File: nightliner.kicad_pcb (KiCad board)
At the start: 2 copper layers, 79 parts, among them J1 TYPE-C-31-M-12, J2 Battery, SW1 SW_SPST, SW10 SW_SPST, SW11 SW_SPST, SW12 SW_SPST, SW13 SW_SPST, SW14 SW_SPST, SW15 SW_SPST, SW16 SW_SPST, SW17 SW_SPST, SW18 SW_SPST, SW19 SW_SPST, SW2 SW_SPST, SW20 SW_SPST, SW21 ON_OFF, SW22 RESET, SW23 BAT_CHECK, SW3 SW_SPST, SW4 SW_SPST, SW5 SW_SPST, SW6 SW_SPST, SW7 SW_SPST, SW8 SW_SPST, SW9 SW_SPST, U1 holyiot-18010, U2 TVS2200DRV, U3 USBLC6-2SC6, U4 BQ24075RGT, U5 XC6220B331MR

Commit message: feat: PCB placement (with wrong choc pos)
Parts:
- removed SW23: BAT_CHECK, miro_keyboard:SW_Push_1P1T_NO_CK_KSC4xxJ
- FB1: value Ferritebead -> Ferrite
- J2: footprint Connector_JST:JST_EH_B3B-EH-A_1x03_P2.50mm_Vertical -> Connector_JST:JST_EH_S3B-EH_1x03_P2.50mm_Horizontal
- SW21: footprint Button_Switch_SMD:SW_SPDT_PCM12 -> miro_keyboard:SW_XKB_SS-12D11_SPDT_Angled
- moved SW9 94.9 mm to (129.2, 69.1), turned to 0 degrees
- moved SW4 88.9 mm to (129.2, 50.9), turned to 0 degrees
- moved D20 87.5 mm to (155.4, 26.7), turned to 90 degrees
- moved SW11 86.9 mm to (33.9, 81.0), turned to 10 degrees
- moved D19 82.1 mm to (151.9, 26.7), turned to 90 degrees
- moved D15 81.6 mm to (155.4, 22.9), turned to 90 degrees
- moved D18 79.4 mm to (148.3, 26.7), turned to 90 degrees
- moved D16 78.3 mm to (141.2, 26.7), turned to 90 degrees
- moved D14 76.2 mm to (151.9, 22.9), turned to 90 degrees
- moved D10 75.8 mm to (155.4, 19.1), turned to 90 degrees
- moved SW16 75.6 mm to (37.0, 98.9), turned to 10 degrees
- moved D17 73.9 mm to (144.8, 26.7), turned to 90 degrees
- moved D13 73.0 mm to (148.3, 22.9), turned to 90 degrees
- moved D3 71.7 mm to (148.3, 15.2), turned to 90 degrees
- moved C6 70.1 mm to (162.6, 65.5), turned to 180 degrees
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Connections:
- U1 pad 12: BAT_CHECK -> unconnected-(U1-A2_P0.04-Pad12)
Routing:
- net COL0: track 38.2 -> 0.00 mm
- net COL1: track 38.2 -> 0.00 mm
- net COL2: track 19.1 -> 0.00 mm
- net COL3: track 19.1 -> 0.00 mm

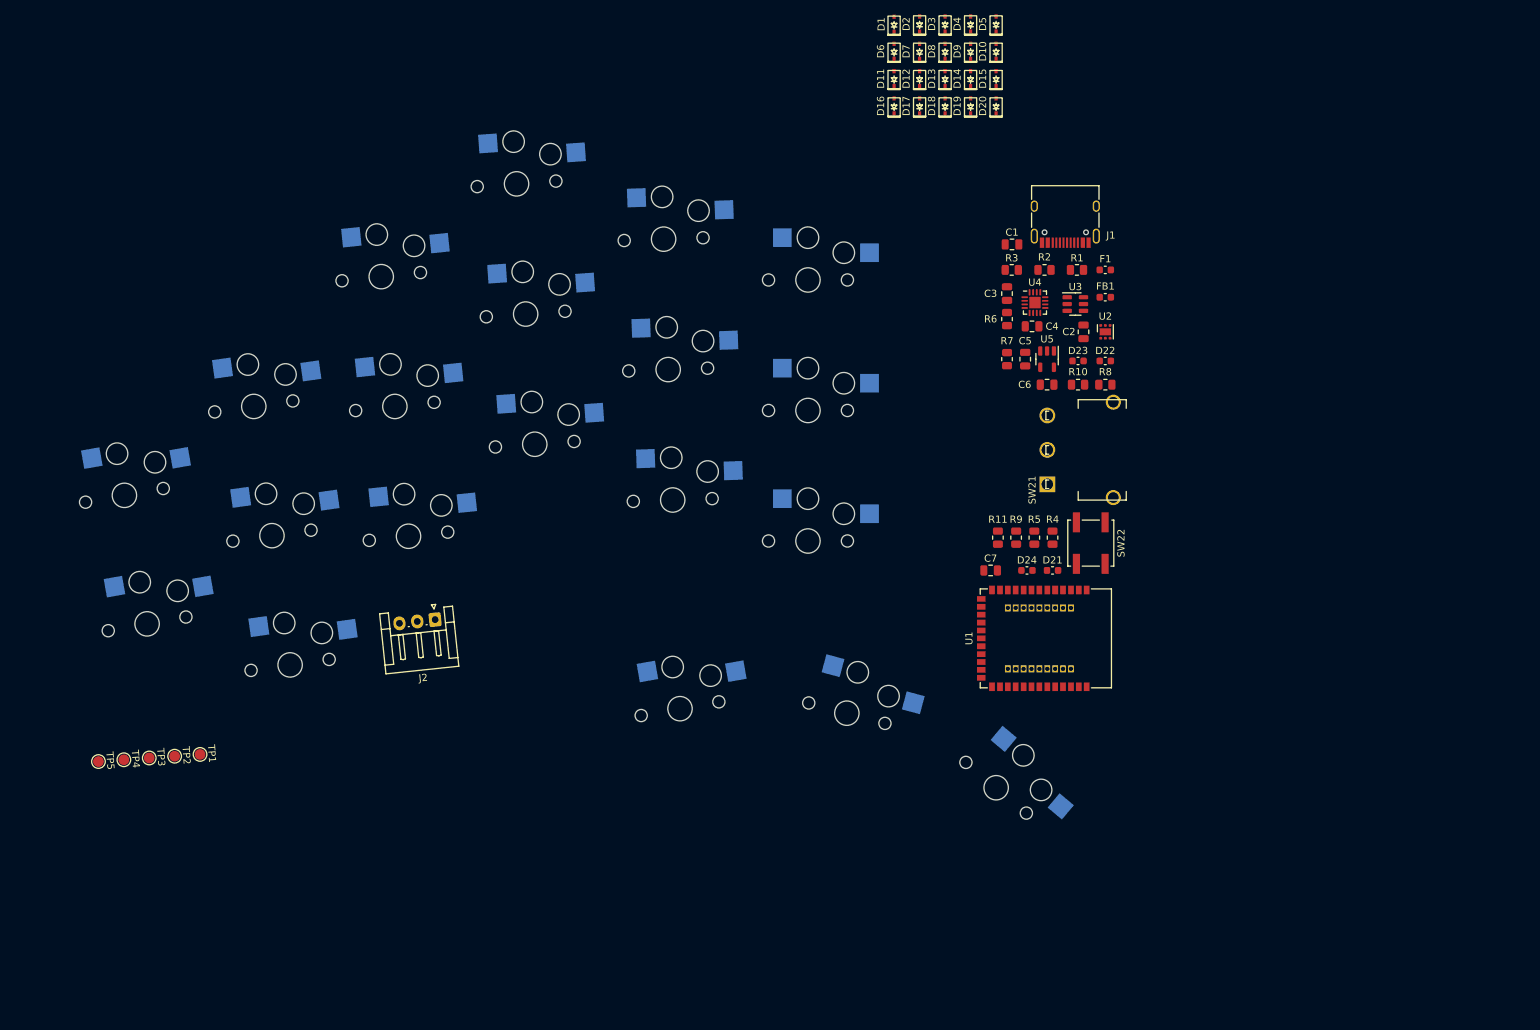
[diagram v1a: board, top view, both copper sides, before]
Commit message: feat: routed PCB, ready for fills
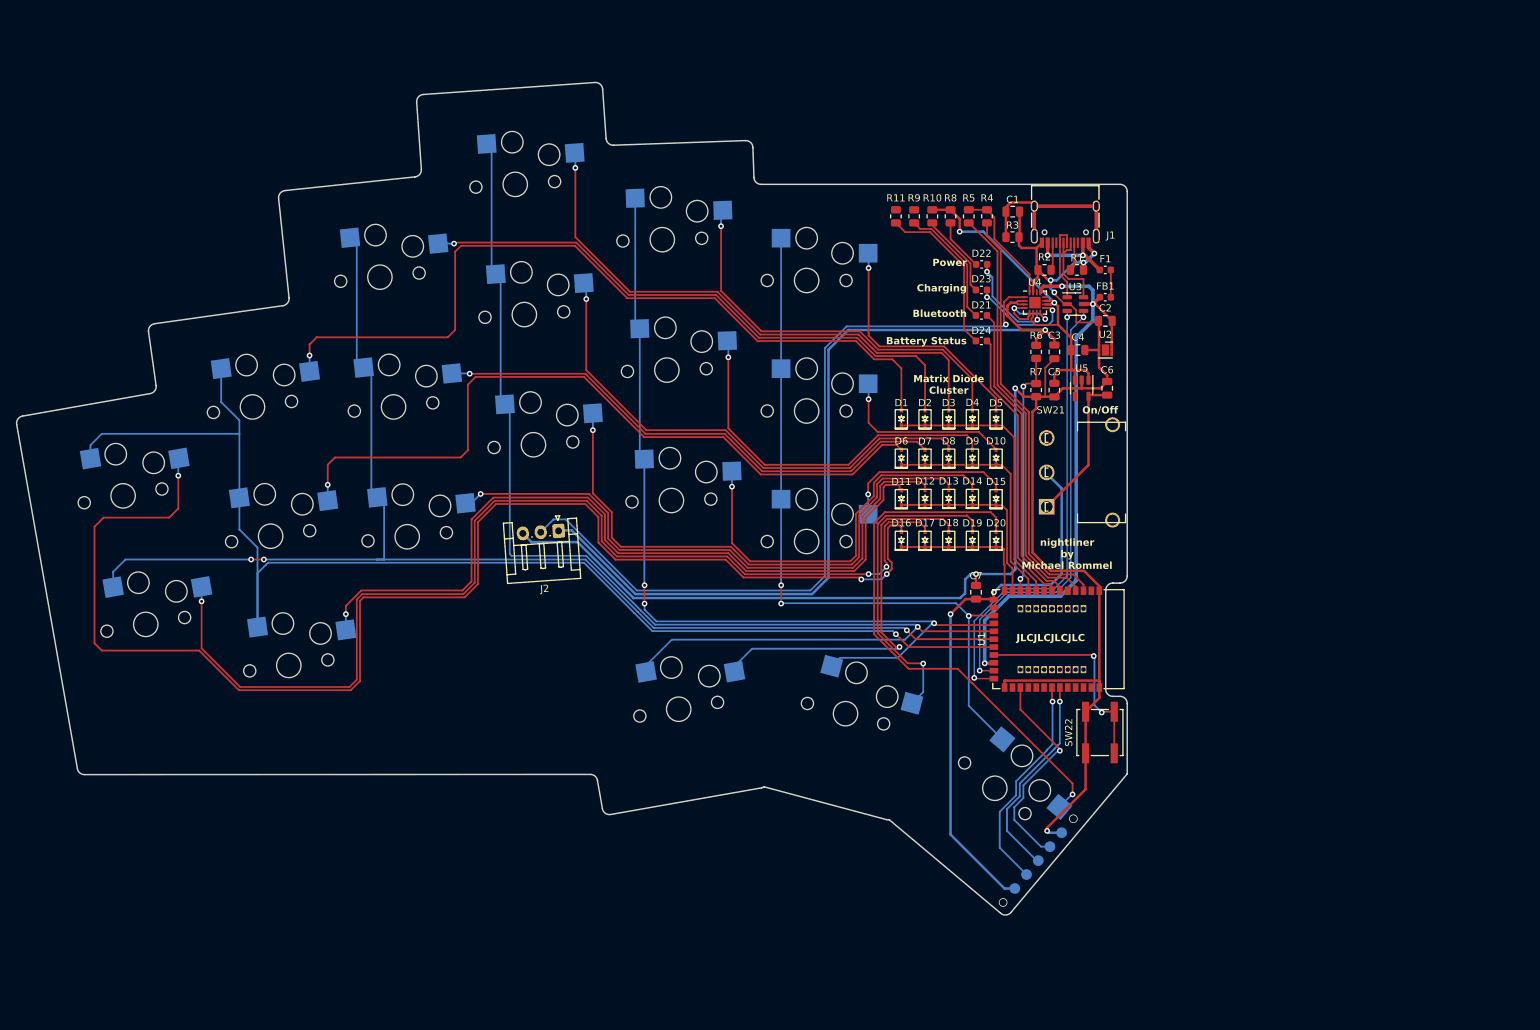
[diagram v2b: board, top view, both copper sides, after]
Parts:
- SW1: value SW_SPST -> pinky_top
- SW10: value SW_SPST -> inner_home
- SW11: value SW_SPST -> pinky_bottom
- SW12: renamed from SW13; value SW_SPST -> ring_bottom
- SW13: renamed from SW15; value SW_SPST -> middle_bottom
- SW14: renamed from SW17; value SW_SPST -> index_bottom
- SW15: renamed from SW19; value SW_SPST -> inner_bottom
- SW16: renamed from SW12; value SW_SPST -> outer_top
- SW17: renamed from SW14; value SW_SPST -> outer_home
- SW18: renamed from SW16; value SW_SPST -> near_thumb
- SW19: renamed from SW18; value SW_SPST -> home_thumb
- SW2: value SW_SPST -> ring_top
- SW20: value SW_SPST -> far_thumb
- SW3: value SW_SPST -> middle_top
- SW4: value SW_SPST -> index_top
- SW5: value SW_SPST -> inner_top
- SW6: value SW_SPST -> pinky_home
- SW7: value SW_SPST -> ring_home
- SW8: value SW_SPST -> middle_home
- SW9: value SW_SPST -> index_home
- TP1, TP2, TP3, TP4, TP5: moved to B.Cu
- moved TP5 134.7 mm to (164.6, 128.0), turned to -40 degrees
- moved TP4 129.7 mm to (163.0, 130.0), turned to -40 degrees
- moved TP3 124.8 mm to (161.3, 131.9), turned to -40 degrees
- moved TP2 119.9 mm to (159.7, 133.9), turned to -40 degrees
- moved TP1 115.2 mm to (158.1, 135.8), turned to -40 degrees
- moved SW16 76.7 mm to (33.7, 81.0), turned to 10 degrees
- moved SW18 75.1 mm to (111.2, 110.8)
- moved D17 64.6 mm to (145.5, 87.1)
- moved D16 64.3 mm to (142.2, 87.1)
- moved D18 60.9 mm to (148.8, 87.1)
- moved D19 60.6 mm to (152.1, 87.1)
- moved D20 60.5 mm to (155.4, 87.1)
- moved SW6 60.1 mm to (54.3, 86.7), turned to 8 degrees
- moved D13 58.8 mm to (148.8, 81.3)
- moved D12 58.5 mm to (145.5, 81.3)
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- renumbered D13 to D12, D15 to D13, D17 to D14, D19 to D15, D12 to D16, D14 to D17, D16 to D18, D18 to D19
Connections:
- U1 pad 10: unconnected-(U1-[L]_A6_P0.30-Pad10) -> ROW1
- U1 pad 12: unconnected-(U1-A2_P0.04-Pad12) -> ROW2
- U1 pad 13: BAT_STAT -> ROW3
- U1 pad 33: ROW0 -> unconnected-(U1-[L]_P0.10-Pad33)
- U1 pad 34: ROW1 -> unconnected-(U1-[L]_P0.09-Pad34)
- U1 pad 35: ROW2 -> unconnected-(U1-[L]_P1.06-Pad35)
- U1 pad 36: ROW3 -> unconnected-(U1-[L]_P1.04-Pad36)
- U1 pad 49: COL4 -> COL0
- U1 pad 5: BT_LED -> unconnected-(U1-[L]_P1.15-Pad5)
- U1 pad 50: COL3 -> COL1
- U1 pad 52: COL1 -> COL3
- U1 pad 53: COL0 -> COL4
- U1 pad 6: unconnected-(U1-[L]_A1_P0.03-Pad6) -> BT_LED
- U1 pad 7: unconnected-(U1-[L]_A0_P0.02-Pad7) -> BAT_STAT
- U1 pad 9: unconnected-(U1-[L]_A5_P0.29-Pad9) -> ROW0
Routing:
- net GND: track 0.00 -> 272.3 mm, vias 0 -> 9
- net Net-(D16-A): track 0.00 -> 188.1 mm, vias 0 -> 3
- net COL1: track 0.00 -> 178.1 mm, vias 0 -> 3
- net COL0: track 0.00 -> 177.1 mm, vias 0 -> 1
- net COL2: track 0.00 -> 171.5 mm, vias 0 -> 1
- net Net-(D17-A): track 0.00 -> 148.0 mm, vias 0 -> 3
- net COL3: track 0.00 -> 124.7 mm, vias 0 -> 3
- net /VBAT: track 0.00 -> 123.0 mm, vias 0 -> 1
- net Net-(D1-A): track 0.00 -> 111.3 mm, vias 0 -> 1
- net /BAT_TEMP: track 0.00 -> 110.1 mm, vias 0 -> 1
- net Net-(D11-A): track 0.00 -> 108.5 mm, vias 0 -> 1
- net Net-(D6-A): track 0.00 -> 103.1 mm, vias 0 -> 1
- net COL4: track 0.00 -> 100.6 mm, vias 0 -> 3
- net VBUS: track 0.00 -> 83.0 mm, vias 0 -> 3
- net Net-(D2-A): track 0.00 -> 81.3 mm, vias 0 -> 1
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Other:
- board outline added: 154.9 x 116.1 mm
- board text added: "Battery Status"
- board text added: "Bluetooth"
- board text added: "Charging"
- board text added: "GND"
- board text added: "JLCJLCJLCJLC"
- board text added: "Matrix Diode Cluster"
- board text added: "On/Off"
- board text added: "Power"
- board text added: "SWCLK"
- board text added: "SWDIO"
- board text added: "SWO"
- board text added: "VDD"
- board text added: "nightliner by Michael Rommel"

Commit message: fix: DRC errors, updated footprints
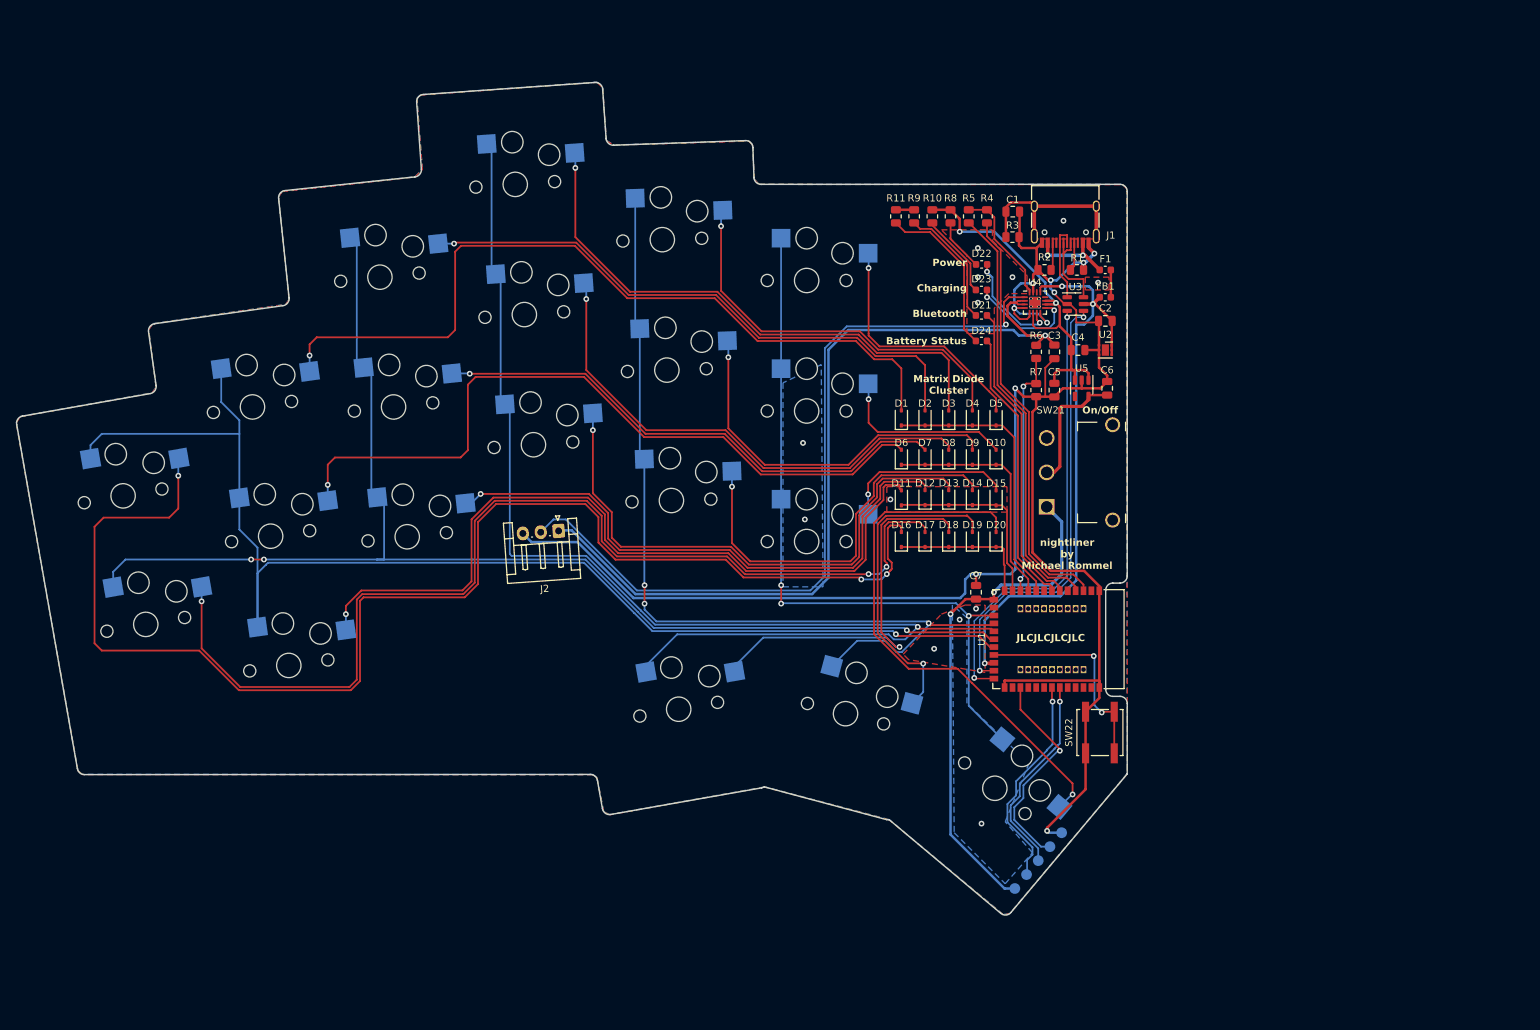
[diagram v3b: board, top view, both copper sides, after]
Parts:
- D1, D10, D11, D12, D13, D14, D15, D16, D17, D18, D19, D2, D20, D3, D4, D5, D6, D7, D8, D9: footprint keebio:D_SOD-323 -> Diode_SMD:D_SOD-323
- U4: footprint Package_DFN_QFN:VQFN-16-1EP_3x3mm_P0.5mm_EP1.6x1.6mm -> miro_keyboard:VQFN-16-1EP_3x3mm_P0.5mm_EP1.6x1.6mm_ThermalVias
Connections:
- C6 pad 1: Net-(SW21-A) -> Net-(SW21-B)
- SW21 pad 1: Net-(SW21-A) -> VDD
- SW21 pad 2: VDD -> Net-(SW21-B)
- SW21 pad 3: (no net) -> unconnected-(SW21-C-Pad3)
- U5 pad 5: Net-(SW21-A) -> Net-(SW21-B)
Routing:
- net Net-(SW21-A): track 20.5 -> 0.00 mm
- net Net-(SW21-B): track 0.00 -> 18.1 mm
- net GND: track 272.3 -> 281.4 mm, vias 9 -> 23
- net VDD: track 76.3 -> 71.5 mm
- net VIN: track 50.6 -> 52.6 mm
- net Net-(D18-A): track 54.3 -> 55.4 mm
- net Net-(D22-K): track 13.6 -> 14.7 mm
- net Net-(D23-K): track 14.6 -> 15.6 mm
- net /VBAT: track 123.0 -> 122.1 mm
- net VBUS: track 83.0 -> 83.7 mm
- net COL3: track 124.7 -> 125.4 mm
- net D-: track 62.5 -> 63.1 mm
- net COL2: track 171.5 -> 172.1 mm
- net SWDIO: track 29.1 -> 28.6 mm
- net (no net): vias 2 -> 0
- added copper zone on B.Cu, net GND
- added copper zone on F.Cu, net GND

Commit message: feat: add mounting holes, better labels
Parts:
- added H1: Alignmenthole, miro_keyboard:Hole_1mm, F.Cu at (166.2, 126.1)
- added H2: Alignmenthole, miro_keyboard:Hole_1mm, F.Cu at (156.4, 137.7)
- added H3: MountingHole_M3, MountingHole:MountingHole_3.2mm_M3, F.Cu at (44.5, 87.1)
- added H4: MountingHole_M3, MountingHole:MountingHole_3.2mm_M3, F.Cu at (81.8, 78.2)
- added H5: MountingHole_M3, MountingHole:MountingHole_3.2mm_M3, F.Cu at (120.7, 62.0)
- added H6: MountingHole_M3, MountingHole:MountingHole_3.2mm_M3, F.Cu at (59.4, 57.4)
- added H7: MountingHole_M3, MountingHole:MountingHole_3.2mm_M3, F.Cu at (99.1, 43.7)
- added H8: MountingHole_M3, MountingHole:MountingHole_3.2mm_M3, F.Cu at (103.9, 100.8)
- added H9: MountingHole_M3, MountingHole:MountingHole_3.2mm_M3, F.Cu at (145.0, 115.6)
- added kibuzzard-653A69A4: G***, kibuzzard-653A69A4, B.Cu at (161.7, 125.6)
- added kibuzzard-653A69BD: G***, kibuzzard-653A69BD, B.Cu at (160.0, 127.5)
- added kibuzzard-653A69C5: G***, kibuzzard-653A69C5, B.Cu at (157.8, 129.0)
- added kibuzzard-653A69CD: G***, kibuzzard-653A69CD, B.Cu at (156.2, 130.9)
- added kibuzzard-653A69D7: G***, kibuzzard-653A69D7, B.Cu at (155.1, 133.3)
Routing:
- net Net-(D9-A): track 51.7 -> 51.1 mm
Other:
- board text removed: "GND"
- board text removed: "SWCLK"
- board text removed: "SWDIO"
- board text removed: "SWO"
- board text removed: "VDD"
